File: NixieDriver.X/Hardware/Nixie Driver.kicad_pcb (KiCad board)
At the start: 2 copper layers, 21.1 x 31.8 mm, 18 parts, among them J1 HDR-2X3, J2 HDR-2X3, Q0 MMBTA42LT1G, Q1 MMBTA42LT1G, Q10 MMBTA42LT1G, Q2 MMBTA42LT1G, Q3 MMBTA42LT1G, Q4 MMBTA42LT1G, Q5 MMBTA42LT1G, Q6 MMBTA42LT1G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

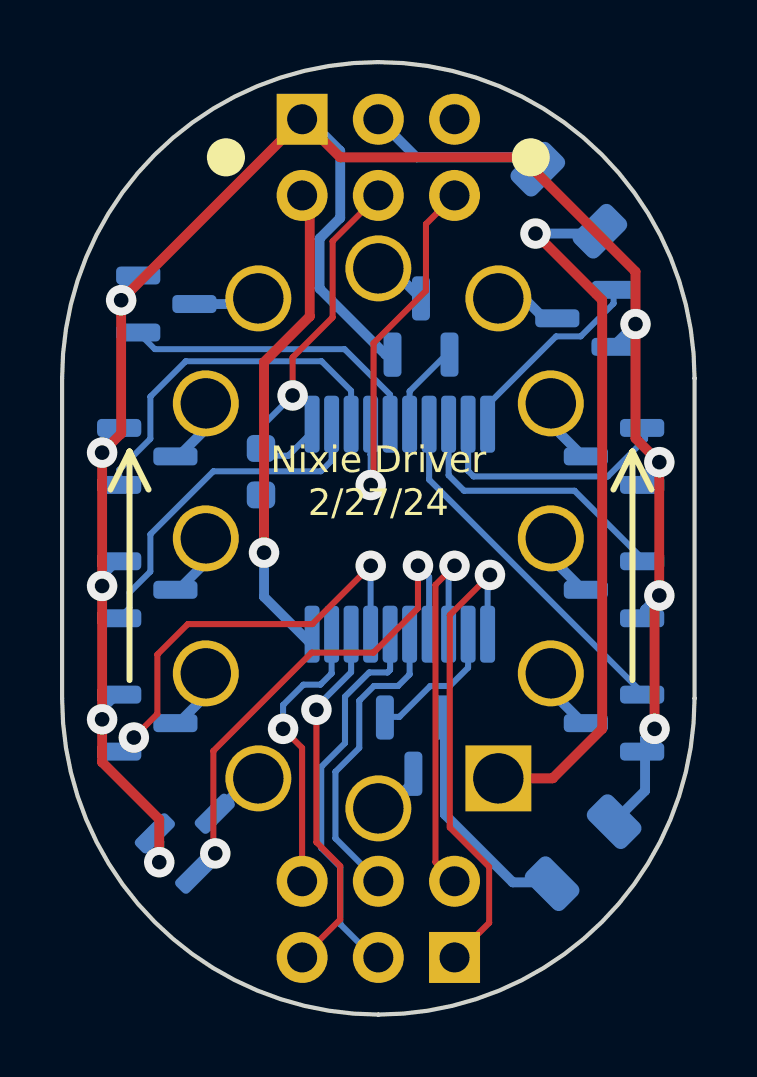
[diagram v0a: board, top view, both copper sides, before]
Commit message: Squashed commit of the following:
commit ceaeb3480282281a1da8399835ad34ef6f77221f
Author: Fish-in-a-Barrel <aaron.m.johnson@gmail.com>
Date:   Tue Dec 17 16:05:15 2024 -0600

    Fixed stencil alignment holes.

commit 4ecd21d86c7d5893fedbf0090fcecf692d6aaa64
Author: Fish-in-a-Barrel <aaron.m.johnson@gmail.com>
Date:   Tue Dec 17 15:40:31 2024 -0600

    Reduced resistor size to 0805

commit 0f75641f3a121fcc031c4463333a2dd006798184
Author: Fish-in-a-Barrel <aaron.m.johnson@gmail.com>
Date:   Tue Dec 17 15:28:49 2024 -0600

    drc updates

commit d9341e6379937dfeab207db1969b1642027c2ff2
Author: Fish-in-a-Barrel <aaron.m.johnson@gmail.com>
Date:   Tue Dec 17 15:04:29 2024 -0600

    Minimal fix for missing current limiting resistor
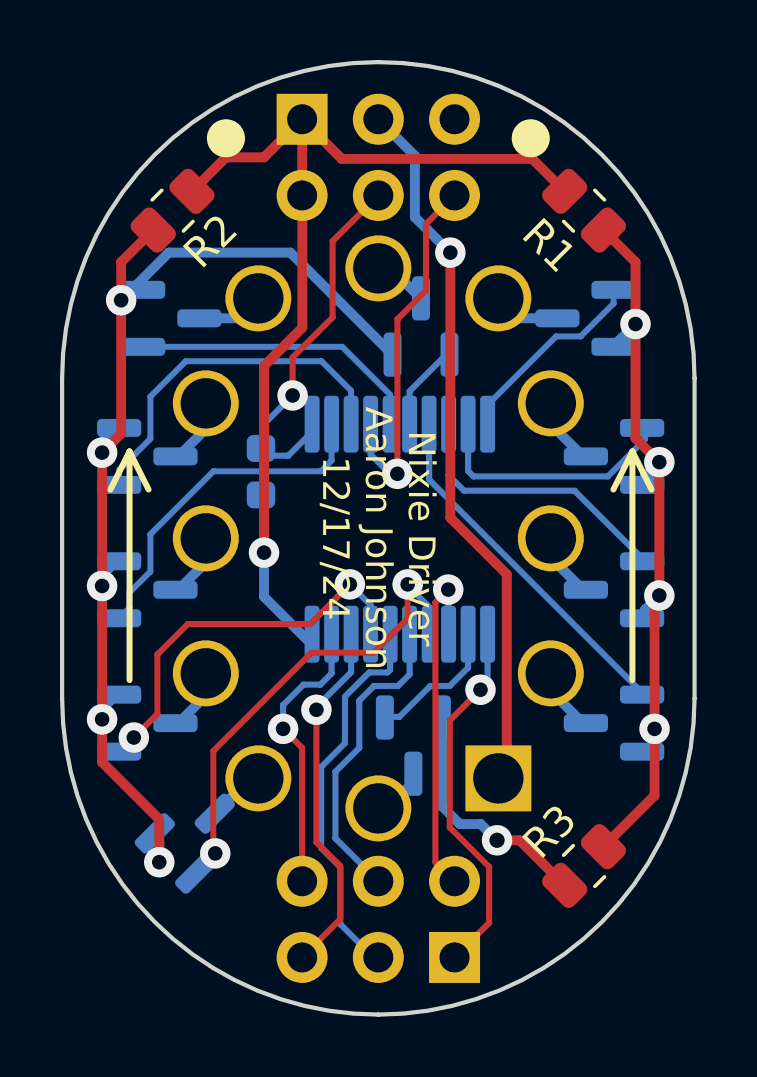
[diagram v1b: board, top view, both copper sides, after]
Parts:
- added R2: 20k, Resistor_SMD:R_0805_2012Metric, F.Cu at (145.5, 90.7)
- J1, J2: value HDR-2X3 -> Conn_02x03_Odd_Even
- R1: value 75 -> 20k; footprint Resistor_SMD:R_1206_3216Metric -> Resistor_SMD:R_0805_2012Metric; moved to F.Cu
- R3: value 15k -> 75k; footprint Resistor_SMD:R_1206_3216Metric -> Resistor_SMD:R_0805_2012Metric; moved to F.Cu
- moved R3 22.2 mm to (159.3, 112.5), turned to -135 degrees
- moved R1 21.4 mm to (159.3, 90.7), turned to 135 degrees
- moved Q5 0.50 mm to (145.5, 94.3)
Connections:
- J1 pad 1: N_GND -> GND
- R1 pad 2: Net-(Q10-E) -> GND
- R3 pad 1: Vnn -> N_GND
- R3 pad 2: Net-(V1-V+) -> Net-(Q10-E)
- V1 pad 1: Net-(V1-V+) -> Vnn
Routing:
- net Net-(V1-V+): track 23.7 -> 0.00 mm, vias 1 -> 0
- net Vnn: track 6.07 -> 23.9 mm, vias 0 -> 1
- net GND: track 18.9 -> 35.4 mm
- net N_GND: track 78.8 -> 63.6 mm
- net /SDA: track 16.7 -> 12.0 mm
- net /SCL: track 13.8 -> 12.0 mm
- net /Driver_2: track 14.4 -> 13.1 mm
- net /Driver_1: track 17.5 -> 16.2 mm
- net /~{MCLR}: track 12.6 -> 12.0 mm
- net Net-(Q10-E): track 7.81 -> 8.14 mm, vias 0 -> 1
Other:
- board text added: "Nixie Driver Aaron Johnson 12/17/24"
- board text removed: "Nixie Driver 2/27/24"

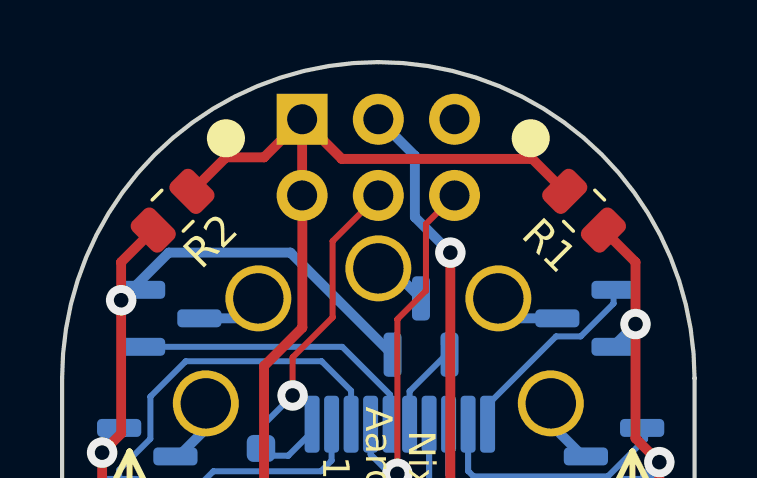
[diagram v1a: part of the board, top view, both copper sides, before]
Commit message: Separated the grounds so the test harness will still work.
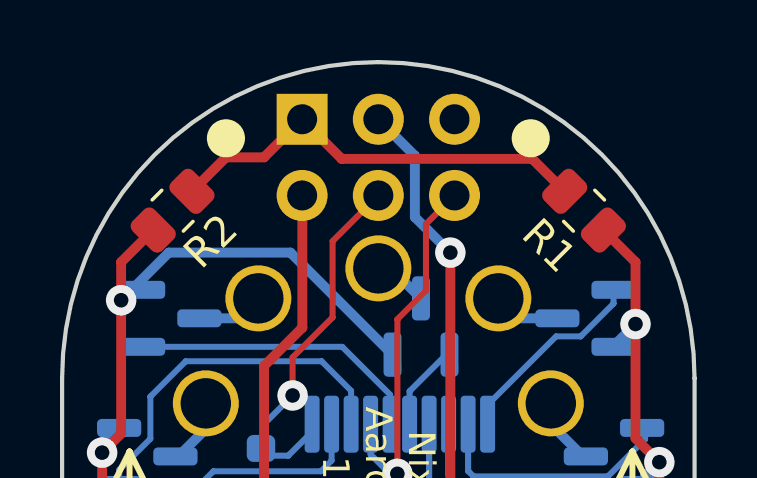
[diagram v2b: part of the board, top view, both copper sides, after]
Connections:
- J1 pad 1: GND -> Net-(J1-Pin_1)
- R1 pad 2: GND -> Net-(J1-Pin_1)
- R2 pad 2: GND -> Net-(J1-Pin_1)
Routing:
- net GND: track 35.4 -> 18.7 mm
- net Net-(J1-Pin_1): track 0.00 -> 14.4 mm
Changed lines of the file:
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@@
 	(net 34 "/SCL")
 	(net 35 "/SDA")
+	(net 36 "Net-(J1-Pin_1)")
 	(footprint "Nixie Driver:IN-12[A_B]"
 		(layer "F.Cu")
@@
 			(layers "F.Cu" "F.Paste" "F.Mask")
 			(roundrect_rratio 0.243902)
-			(net 1 "GND")
+			(net 36 "Net-(J1-Pin_1)")
 			(pintype "passive")
 		)
@@
 			(layers "F.Cu" "F.Paste" "F.Mask")
 			(roundrect_rratio 0.243902)
-			(net 1 "GND")
+			(net 36 "Net-(J1-Pin_1)")
 			(pintype "passive")
 		)
@@
 			(layers "*.Cu" "*.Mask")
 			(remove_unused_layers no)
-			(net 1 "GND")
+			(net 36 "Net-(J1-Pin_1)")
 			(pinfunction "Pin_1")
 			(pintype "passive")
@@
 	)
 	(segment
-		(start 157.5318 88.9518)
-		(end 151.1818 88.9518)
-		(width 0.33)
-		(layer "F.Cu")
-		(net 1)
-	)
-	(segment
-		(start 149.86 90.17)
-		(end 149.86 88.384058)
-		(width 0.33)
-		(layer "F.Cu")
-		(net 1)
-	)
-	(segment
-		(start 148.59 88.9)
-		(end 149.86 87.63)
-		(width 0.33)
-		(layer "F.Cu")
-		(net 1)
-	)
-	(segment
 		(start 149.8682 94.577402)
 		(end 148.59 95.855602)
@@
 	)
 	(segment
-		(start 151.1818 88.9518)
-		(end 149.86 87.63)
-		(width 0.33)
-		(layer "F.Cu")
-		(net 1)
-	)
-	(segment
-		(start 147.32 88.9)
-		(end 148.59 88.9)
-		(width 0.33)
-		(layer "F.Cu")
-		(net 1)
-	)
-	(segment
 		(start 148.59 95.855602)
 		(end 148.59 102.076267)
@@
 	)
 	(segment
-		(start 149.86 88.384058)
-		(end 150.237029 88.007029)
-		(width 0.33)
-		(layer "F.Cu")
-		(net 1)
-	)
-	(segment
 		(start 149.8682 90.1782)
 		(end 149.8682 94.577402)
@@
 	)
 	(segment
-		(start 158.612765 90.032765)
-		(end 157.5318 88.9518)
-		(width 0.33)
-		(layer "F.Cu")
-		(net 1)
-	)
-	(segment
-		(start 146.187235 90.032765)
-		(end 147.32 88.9)
-		(width 0.33)
-		(layer "F.Cu")
-		(net 1)
-	)
-	(segment
 		(start 149.86 90.17)
 		(end 149.8682 90.1782)
@@
 		(net 35)
 	)
+	(segment
+		(start 157.5318 88.9518)
+		(end 151.1818 88.9518)
+		(width 0.33)
+		(layer "F.Cu")
+		(net 36)
+	)
+	(segment
+		(start 148.59 88.9)
+		(end 149.86 87.63)
+		(width 0.33)
+		(layer "F.Cu")
+		(net 36)
+	)
+	(segment
+		(start 151.1818 88.9518)
+		(end 149.86 87.63)
+		(width 0.33)
+		(layer "F.Cu")
+		(net 36)
+	)
+	(segment
+		(start 147.32 88.9)
+		(end 148.59 88.9)
+		(width 0.33)
+		(layer "F.Cu")
+		(net 36)
+	)
+	(segment
+		(start 158.612765 90.032765)
+		(end 157.5318 88.9518)
+		(width 0.33)
+		(layer "F.Cu")
+		(net 36)
+	)
+	(segment
+		(start 146.187235 90.032765)
+		(end 147.32 88.9)
+		(width 0.33)
+		(layer "F.Cu")
+		(net 36)
+	)
 	(group ""

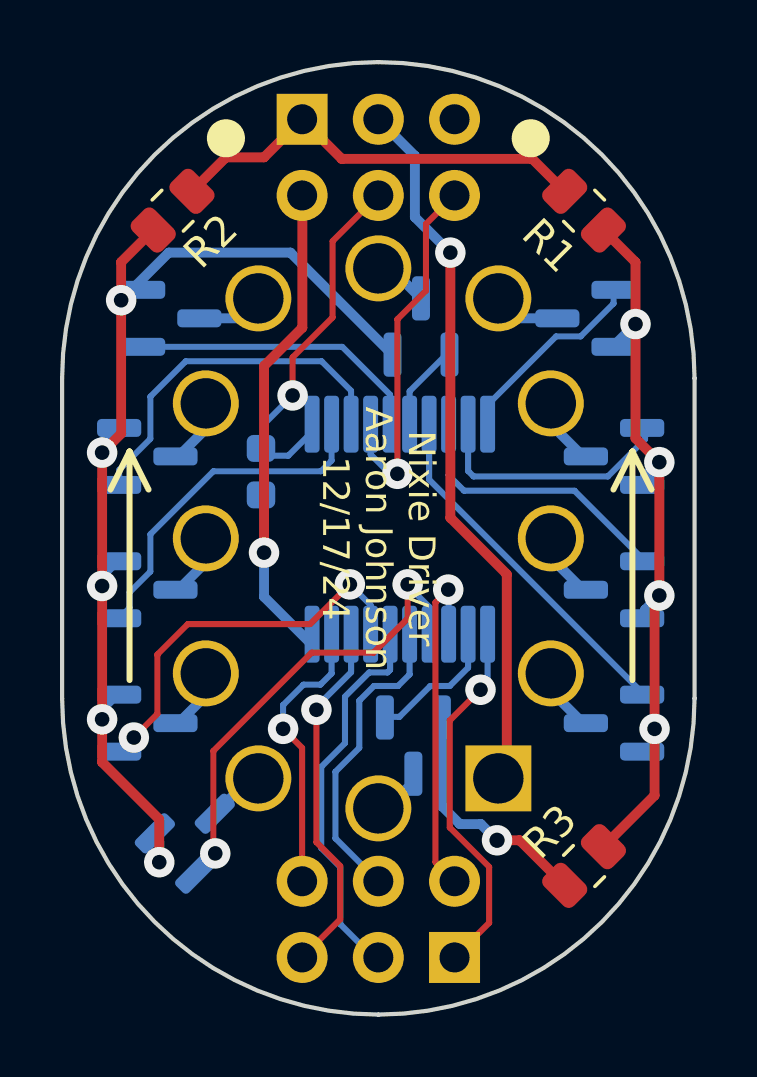
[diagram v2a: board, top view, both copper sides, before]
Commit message: Move resistor back to the anode
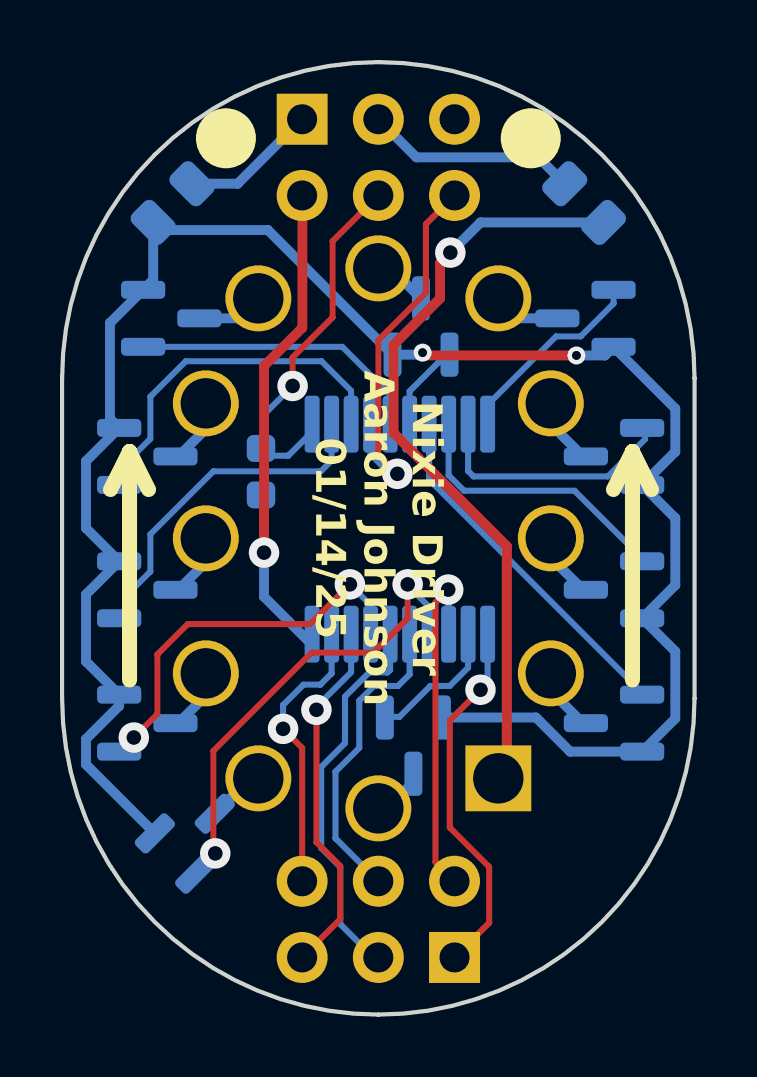
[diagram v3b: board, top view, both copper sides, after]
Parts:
- removed R3: 75k, Resistor_SMD:R_0805_2012Metric
- R1: moved to B.Cu
- R2: value 20k -> 2.2k; moved to B.Cu
- moved R1 0.25 mm to (159.3, 90.4)
- moved R2 0.25 mm to (145.5, 90.4)
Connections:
- Q10 pad 2: Net-(Q10-E) -> N_GND
- R1 pad 1: N_GND -> Net-(V1-V+)
- R1 pad 2: Net-(J1-Pin_1) -> Vnn
- V1 pad 1: Vnn -> Net-(V1-V+)
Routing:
- net Net-(V1-V+): track 0.00 -> 25.5 mm, vias 0 -> 1
- net Vnn: track 23.9 -> 7.10 mm, vias 1 -> 0
- net Net-(J1-Pin_1): track 14.4 -> 4.56 mm
- net Net-(Q10-E): track 8.14 -> 0.00 mm, vias 1 -> 0
- net N_GND: track 63.6 -> 65.5 mm, vias 9 -> 2
- net /~{MCLR}: track 12.0 -> 12.5 mm
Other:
- board text added: "Nixie Driver Aaron Johnson 01/14/25"
- board text removed: "Nixie Driver Aaron Johnson 12/17/24"

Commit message: Cleaned up traces.
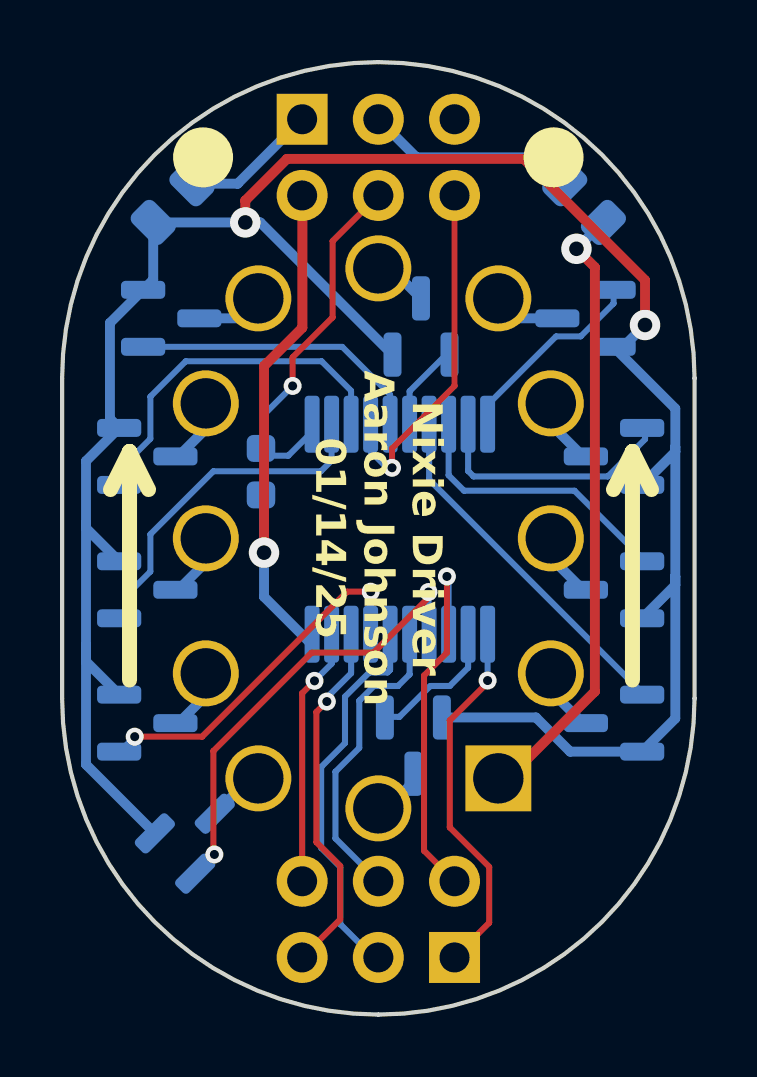
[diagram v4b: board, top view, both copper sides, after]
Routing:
- net N_GND: track 65.5 -> 80.8 mm
- net Net-(V1-V+): track 25.5 -> 20.7 mm
- net /SCL: track 12.0 -> 13.2 mm
- net /Driver_2: track 13.1 -> 12.0 mm
- net /ADDR0/DAT: track 9.14 -> 8.29 mm
- net /~{MCLR}: track 12.5 -> 11.8 mm
- net /Driver_1: track 16.2 -> 15.7 mm
